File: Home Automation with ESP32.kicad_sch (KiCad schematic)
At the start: 0 parts

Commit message: Placed MCU (ESP32-WROOM-32) in Schematic
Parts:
- added U1: ESP32-WROOM-32, RF_Module:ESP32-WROOM-32, symbol RF_Module:ESP32-WROOM-32
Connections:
- new net: U1.1 (GND), U1.15 (GND), U1.38 (GND), U1.39 (GND)
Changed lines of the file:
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@@
 	(generator_version "9.0")
 	(paper "A4")
+	(symbol
+		(lib_id "RF_Module:ESP32-WROOM-32")
+		(at 246.38 68.58 0)
+		(unit 1)
+		(exclude_from_sim no)
+		(in_bom yes)
+		(on_board yes)
+		(dnp no)
+		(fields_autoplaced yes)
+		(property "Reference" "U1"
+			(at 248.5233 30.48 0)
+			(effects
+				(font
+					(size 1.27 1.27)
+				)
+				(justify left)
+			)
+		)
+		(property "Value" "ESP32-WROOM-32"
+			(at 248.5233 33.02 0)
+			(effects
+				(font
+					(size 1.27 1.27)
+				)
+				(justify left)
+			)
+		)
+		(property "Footprint" "RF_Module:ESP32-WROOM-32"
+			(at 246.38 106.68 0)
+			(effects
+				(font
+					(size 1.27 1.27)
+				)
+				(hide yes)
+			)
+		)
+		(property "Datasheet" "https://www.espressif.com/sites/default/files/documentation/esp32-wroom-32_datasheet_en.pdf"
+			(at 238.76 67.31 0)
+			(effects
+				(font
+					(size 1.27 1.27)
+				)
+				(hide yes)
+			)
+		)
+		(property "Description" "RF Module, ESP32-D0WDQ6 SoC, Wi-Fi 802.11b/g/n, Bluetooth, BLE, 32-bit, 2.7-3.6V, onboard antenna, SMD"
+			(at 246.38 68.58 0)
+			(effects
+				(font
+					(size 1.27 1.27)
+				)
+				(hide yes)
+			)
+		)
+		(pin "8"
+		)
+		(pin "23"
+		)
+		(pin "12"
+		)
+		(pin "27"
+		)
+		(pin "28"
+		)
+		(pin "33"
+		)
+		(pin "9"
+		)
+		(pin "7"
+		)
+		(pin "11"
+		)
+		(pin "36"
+		)
+		(pin "30"
+		)
+		(pin "10"
+		)
+		(pin "6"
+		)
+		(pin "31"
+		)
+		(pin "37"
+		)
+		(pin "5"
+		)
+		(pin "21"
+		)
+		(pin "22"
+		)
+		(pin "3"
+		)
+		(pin "4"
+		)
+		(pin "16"
+		)
+		(pin "13"
+		)
+		(pin "39"
+		)
+		(pin "32"
+		)
+		(pin "17"
+		)
+		(pin "20"
+		)
+		(pin "15"
+		)
+		(pin "24"
+		)
+		(pin "1"
+		)
+		(pin "34"
+		)
+		(pin "29"
+		)
+		(pin "14"
+		)
+		(pin "18"
+		)
+		(pin "25"
+		)
+		(pin "2"
+		)
+		(pin "38"
+		)
+		(pin "19"
+		)
+		(pin "35"
+		)
+		(pin "26"
+		)
+		(instances
+			(project ""
+				(path "/7438dd54-9f08-4599-aef6-4a86e3e5147b"
+					(reference "U1")
+					(unit 1)
+				)
+			)
+		)
+	)
 	(sheet_instances
 		(path "/"

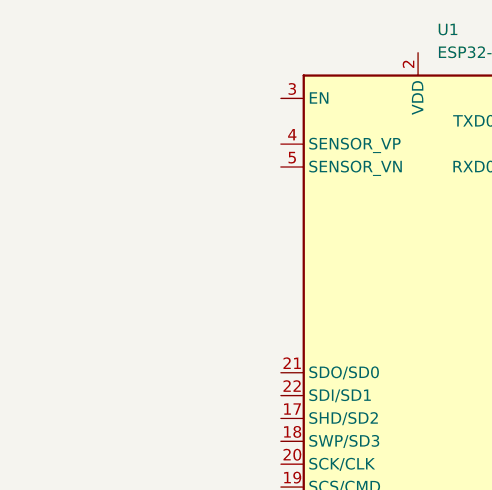
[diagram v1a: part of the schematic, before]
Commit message: Placed Isolator (PC817) in Schematic
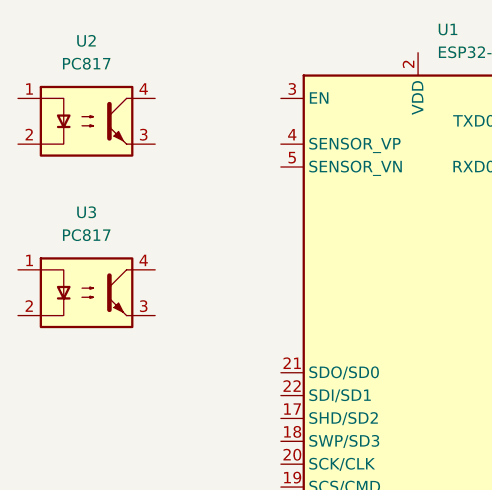
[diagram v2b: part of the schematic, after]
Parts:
- added U2, U3: PC817, Package_DIP:DIP-4_W7.62mm, symbol Isolator:PC817
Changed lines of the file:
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@@
 	(paper "A4")
+	(symbol
+		(lib_id "Isolator:PC817")
+		(at 209.55 40.64 0)
+		(unit 1)
+		(exclude_from_sim no)
+		(in_bom yes)
+		(on_board yes)
+		(dnp no)
+		(fields_autoplaced yes)
+		(property "Reference" "U2"
+			(at 209.55 31.75 0)
+			(effects
+				(font
+					(size 1.27 1.27)
+				)
+			)
+		)
+		(property "Value" "PC817"
+			(at 209.55 34.29 0)
+			(effects
+				(font
+					(size 1.27 1.27)
+				)
+			)
+		)
+		(property "Footprint" "Package_DIP:DIP-4_W7.62mm"
+			(at 204.47 45.72 0)
+			(effects
+				(font
+					(size 1.27 1.27)
+					(italic yes)
+				)
+				(justify left)
+				(hide yes)
+			)
+		)
+		(property "Datasheet" "http://www.soselectronic.cz/a_info/resource/d/pc817.pdf"
+			(at 209.55 40.64 0)
+			(effects
+				(font
+					(size 1.27 1.27)
+				)
+				(justify left)
+				(hide yes)
+			)
+		)
+		(property "Description" "DC Optocoupler, Vce 35V, CTR 50-300%, DIP-4"
+			(at 209.55 40.64 0)
+			(effects
+				(font
+					(size 1.27 1.27)
+				)
+				(hide yes)
+			)
+		)
+		(pin "3"
+		)
+		(pin "2"
+		)
+		(pin "1"
+		)
+		(pin "4"
+		)
+		(instances
+			(project ""
+				(path "/7438dd54-9f08-4599-aef6-4a86e3e5147b"
+					(reference "U2")
+					(unit 1)
+				)
+			)
+		)
+	)
+	(symbol
+		(lib_id "Isolator:PC817")
+		(at 209.55 59.69 0)
+		(unit 1)
+		(exclude_from_sim no)
+		(in_bom yes)
+		(on_board yes)
+		(dnp no)
+		(fields_autoplaced yes)
+		(property "Reference" "U3"
+			(at 209.55 50.8 0)
+			(effects
+				(font
+					(size 1.27 1.27)
+				)
+			)
+		)
+		(property "Value" "PC817"
+			(at 209.55 53.34 0)
+			(effects
+				(font
+					(size 1.27 1.27)
+				)
+			)
+		)
+		(property "Footprint" "Package_DIP:DIP-4_W7.62mm"
+			(at 204.47 64.77 0)
+			(effects
+				(font
+					(size 1.27 1.27)
+					(italic yes)
+				)
+				(justify left)
+				(hide yes)
+			)
+		)
+		(property "Datasheet" "http://www.soselectronic.cz/a_info/resource/d/pc817.pdf"
+			(at 209.55 59.69 0)
+			(effects
+				(font
+					(size 1.27 1.27)
+				)
+				(justify left)
+				(hide yes)
+			)
+		)
+		(property "Description" "DC Optocoupler, Vce 35V, CTR 50-300%, DIP-4"
+			(at 209.55 59.69 0)
+			(effects
+				(font
+					(size 1.27 1.27)
+				)
+				(hide yes)
+			)
+		)
+		(pin "3"
+		)
+		(pin "2"
+		)
+		(pin "1"
+		)
+		(pin "4"
+		)
+		(instances
+			(project "Home Automation with ESP32"
+				(path "/7438dd54-9f08-4599-aef6-4a86e3e5147b"
+					(reference "U3")
+					(unit 1)
+				)
+			)
+		)
+	)
 	(symbol
 		(lib_id "RF_Module:ESP32-WROOM-32")

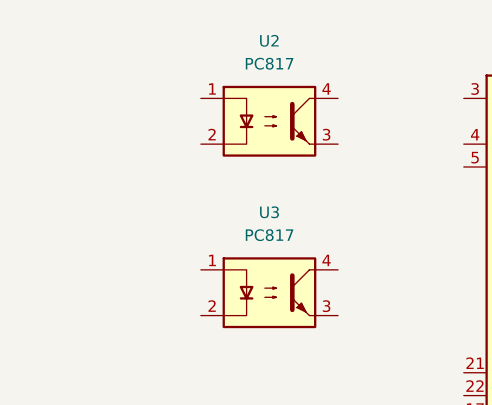
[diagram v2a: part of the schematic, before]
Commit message: Placed Linear Regulator (AMS1117-3.3) in Schematic
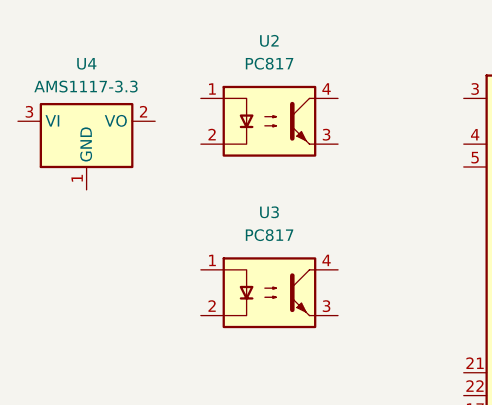
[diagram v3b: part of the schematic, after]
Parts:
- added U4: AMS1117-3.3, Package_TO_SOT_SMD:SOT-223-3_TabPin2, symbol Regulator_Linear:AMS1117-3.3
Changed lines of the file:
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@@
+	)
+	(symbol
+		(lib_id "Regulator_Linear:AMS1117-3.3")
+		(at 189.23 40.64 0)
+		(unit 1)
+		(exclude_from_sim no)
+		(in_bom yes)
+		(on_board yes)
+		(dnp no)
+		(fields_autoplaced yes)
+		(property "Reference" "U4"
+			(at 189.23 34.29 0)
+			(effects
+				(font
+					(size 1.27 1.27)
+				)
+			)
+		)
+		(property "Value" "AMS1117-3.3"
+			(at 189.23 36.83 0)
+			(effects
+				(font
+					(size 1.27 1.27)
+				)
+			)
+		)
+		(property "Footprint" "Package_TO_SOT_SMD:SOT-223-3_TabPin2"
+			(at 189.23 35.56 0)
+			(effects
+				(font
+					(size 1.27 1.27)
+				)
+				(hide yes)
+			)
+		)
+		(property "Datasheet" "http://www.advanced-monolithic.com/pdf/ds1117.pdf"
+			(at 191.77 46.99 0)
+			(effects
+				(font
+					(size 1.27 1.27)
+				)
+				(hide yes)
+			)
+		)
+		(property "Description" "1A Low Dropout regulator, positive, 3.3V fixed output, SOT-223"
+			(at 189.23 40.64 0)
+			(effects
+				(font
+					(size 1.27 1.27)
+				)
+				(hide yes)
+			)
+		)
+		(pin "2"
+		)
+		(pin "3"
+		)
+		(pin "1"
+		)
+		(instances
+			(project ""
+				(path "/7438dd54-9f08-4599-aef6-4a86e3e5147b"
+					(reference "U4")
+					(unit 1)
+				)
+			)
+		)
 	)
 	(symbol

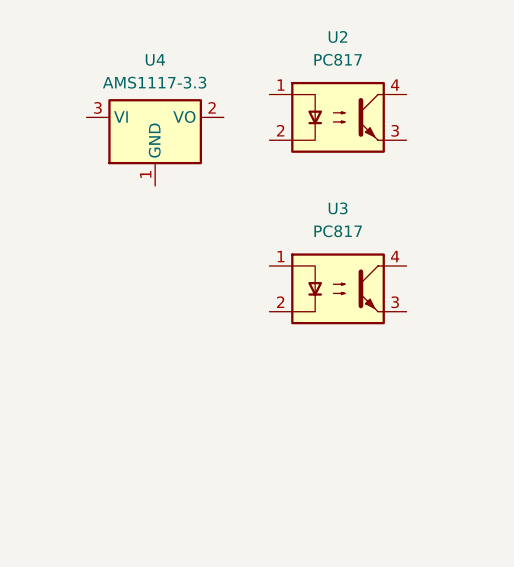
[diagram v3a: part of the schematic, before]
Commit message: Placed AC/DC Converter (HLK-PM01) in Schematic
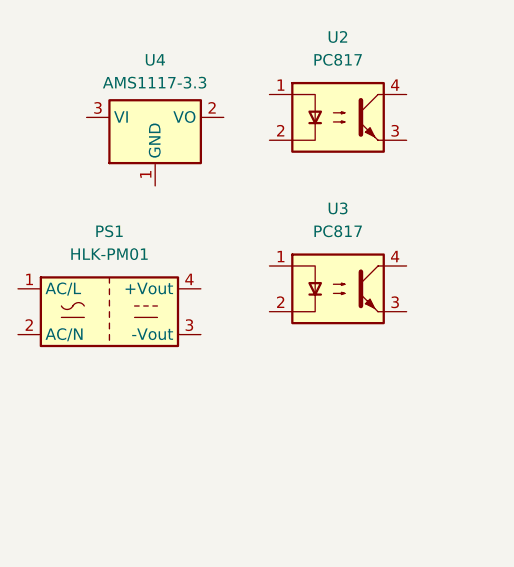
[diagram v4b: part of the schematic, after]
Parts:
- added PS1: HLK-PM01, Converter_ACDC:Converter_ACDC_Hi-Link_HLK-PMxx, symbol Converter_ACDC:HLK-PM01
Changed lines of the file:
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@@
+	)
+	(symbol
+		(lib_id "Converter_ACDC:HLK-PM01")
+		(at 184.15 62.23 0)
+		(unit 1)
+		(exclude_from_sim no)
+		(in_bom yes)
+		(on_board yes)
+		(dnp no)
+		(fields_autoplaced yes)
+		(property "Reference" "PS1"
+			(at 184.15 53.34 0)
+			(effects
+				(font
+					(size 1.27 1.27)
+				)
+			)
+		)
+		(property "Value" "HLK-PM01"
+			(at 184.15 55.88 0)
+			(effects
+				(font
+					(size 1.27 1.27)
+				)
+			)
+		)
+		(property "Footprint" "Converter_ACDC:Converter_ACDC_Hi-Link_HLK-PMxx"
+			(at 184.15 69.85 0)
+			(effects
+				(font
+					(size 1.27 1.27)
+				)
+				(hide yes)
+			)
+		)
+		(property "Datasheet" "https://h.hlktech.com/download/ACDC%E7%94%B5%E6%BA%90%E6%A8%A1%E5%9D%973W%E7%B3%BB%E5%88%97/1/%E6%B5%B7%E5%87%8C%E7%A7%913W%E7%B3%BB%E5%88%97%E7%94%B5%E6%BA%90%E6%A8%A1%E5%9D%97%E8%A7%84%E6%A0%BC%E4%B9%A6V2.8.pdf"
+			(at 194.31 71.12 0)
+			(effects
+				(font
+					(size 1.27 1.27)
+				)
+				(hide yes)
+			)
+		)
+		(property "Description" "Compact AC/DC board mount power module 3W 5V"
+			(at 184.15 62.23 0)
+			(effects
+				(font
+					(size 1.27 1.27)
+				)
+				(hide yes)
+			)
+		)
+		(pin "1"
+		)
+		(pin "4"
+		)
+		(pin "3"
+		)
+		(pin "2"
+		)
+		(instances
+			(project ""
+				(path "/7438dd54-9f08-4599-aef6-4a86e3e5147b"
+					(reference "PS1")
+					(unit 1)
+				)
+			)
+		)
 	)
 	(symbol

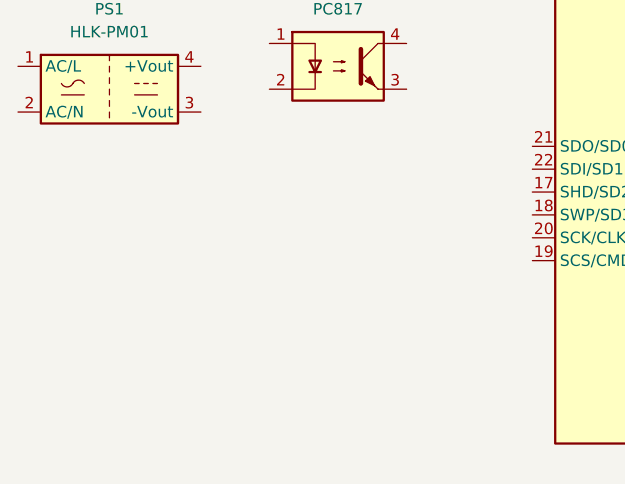
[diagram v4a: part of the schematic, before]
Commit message: Placed Power Relay (RAYEX-L90AS) in Schematic
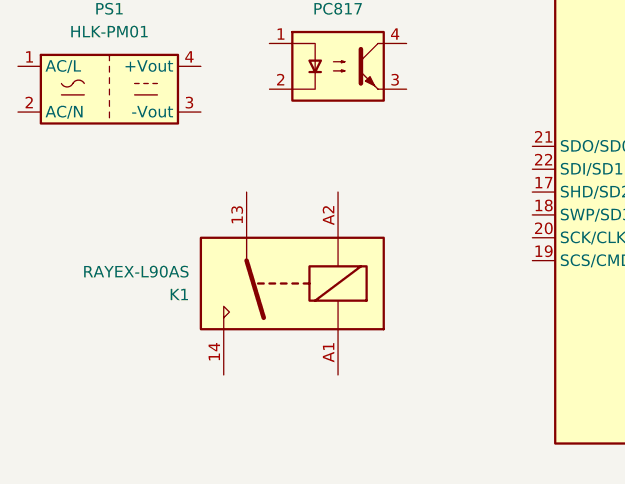
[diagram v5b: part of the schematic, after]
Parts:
- added K1: RAYEX-L90AS, Relay_THT:Relay_SPST_RAYEX-L90AS, symbol Relay:RAYEX-L90AS
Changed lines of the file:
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@@
 	(paper "A4")
+	(symbol
+		(lib_id "Relay:RAYEX-L90AS")
+		(at 204.47 83.82 180)
+		(unit 1)
+		(exclude_from_sim no)
+		(in_bom yes)
+		(on_board yes)
+		(dnp no)
+		(property "Reference" "K1"
+			(at 193.04 85.0901 0)
+			(effects
+				(font
+					(size 1.27 1.27)
+				)
+				(justify left)
+			)
+		)
+		(property "Value" "RAYEX-L90AS"
+			(at 193.04 82.5501 0)
+			(effects
+				(font
+					(size 1.27 1.27)
+				)
+				(justify left)
+			)
+		)
+		(property "Footprint" "Relay_THT:Relay_SPST_RAYEX-L90AS"
+			(at 193.04 82.55 0)
+			(effects
+				(font
+					(size 1.27 1.27)
+				)
+				(justify left)
+				(hide yes)
+			)
+		)
+		(property "Datasheet" "https://a3.sofastcdn.com/attachment/7jioKBjnRiiSrjrjknRiwS77gwbf3zmp/L90-SERIES.pdf"
+			(at 186.69 80.01 0)
+			(effects
+				(font
+					(size 1.27 1.27)
+				)
+				(justify left)
+				(hide yes)
+			)
+		)
+		(property "Description" "Power relay, Without Common Terminal between coil terminals, NO, SPST, 30A"
+			(at 204.47 83.82 0)
+			(effects
+				(font
+					(size 1.27 1.27)
+				)
+				(hide yes)
+			)
+		)
+		(pin "14"
+		)
+		(pin "A1"
+		)
+		(pin "13"
+		)
+		(pin "A2"
+		)
+		(instances
+			(project ""
+				(path "/7438dd54-9f08-4599-aef6-4a86e3e5147b"
+					(reference "K1")
+					(unit 1)
+				)
+			)
+		)
+	)
 	(symbol
 		(lib_id "Isolator:PC817")

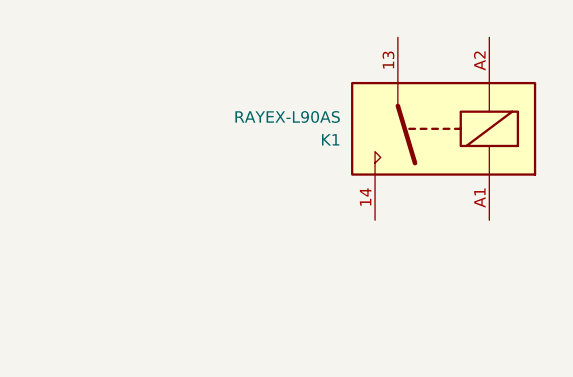
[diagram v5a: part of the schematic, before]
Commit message: Placed SPDT Power Relay (pr13-5v-450-1c) in Schematic
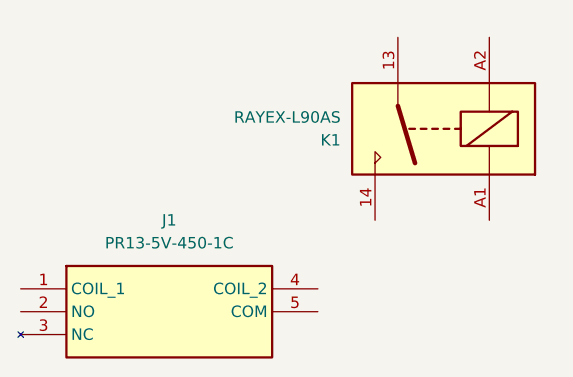
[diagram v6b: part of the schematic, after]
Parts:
- added J1: PR13-5V-450-1C, PR135V4501C, symbol PR13-5V-450-1C:PR13-5V-450-1C
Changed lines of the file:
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@@
+	)
+	(symbol
+		(lib_id "PR13-5V-450-1C:PR13-5V-450-1C")
+		(at 157.48 101.6 0)
+		(unit 1)
+		(exclude_from_sim no)
+		(in_bom yes)
+		(on_board yes)
+		(dnp no)
+		(fields_autoplaced yes)
+		(property "Reference" "J1"
+			(at 173.99 93.98 0)
+			(effects
+				(font
+					(size 1.27 1.27)
+				)
+			)
+		)
+		(property "Value" "PR13-5V-450-1C"
+			(at 173.99 96.52 0)
+			(effects
+				(font
+					(size 1.27 1.27)
+				)
+			)
+		)
+		(property "Footprint" "PR135V4501C"
+			(at 186.69 196.52 0)
+			(effects
+				(font
+					(size 1.27 1.27)
+				)
+				(justify left top)
+				(hide yes)
+			)
+		)
+		(property "Datasheet" "https://www.sameskydevices.com/product/resource/pr13.pdf"
+			(at 186.69 296.52 0)
+			(effects
+				(font
+					(size 1.27 1.27)
+				)
+				(justify left top)
+				(hide yes)
+			)
+		)
+		(property "Description" "19 x 15.5 x 15.8 mm, 5 V, 10 A, SPDT (1 Form C), Power Relay"
+			(at 157.48 101.6 0)
+			(effects
+				(font
+					(size 1.27 1.27)
+				)
+				(hide yes)
+			)
+		)
+		(property "Height" "16.1"
+			(at 186.69 496.52 0)
+			(effects
+				(font
+					(size 1.27 1.27)
+				)
+				(justify left top)
+				(hide yes)
+			)
+		)
+		(property "Manufacturer_Name" "Same Sky"
+			(at 186.69 596.52 0)
+			(effects
+				(font
+					(size 1.27 1.27)
+				)
+				(justify left top)
+				(hide yes)
+			)
+		)
+		(property "Manufacturer_Part_Number" "PR13-5V-450-1C"
+			(at 186.69 696.52 0)
+			(effects
+				(font
+					(size 1.27 1.27)
+				)
+				(justify left top)
+				(hide yes)
+			)
+		)
+		(property "Mouser Part Number" "179-PR13-5V-450-1C"
+			(at 186.69 796.52 0)
+			(effects
+				(font
+					(size 1.27 1.27)
+				)
+				(justify left top)
+				(hide yes)
+			)
+		)
+		(property "Mouser Price/Stock" "https://www.mouser.co.uk/ProductDetail/CUI-Devices/PR13-5V-450-1C?qs=T%252BzbugeAwjjEdhOl%2F9q49A%3D%3D"
+			(at 186.69 896.52 0)
+			(effects
+				(font
+					(size 1.27 1.27)
+				)
+				(justify left top)
+				(hide yes)
+			)
+		)
+		(property "Arrow Part Number" "PR13-5V-450-1C"
+			(at 186.69 996.52 0)
+			(effects
+				(font
+					(size 1.27 1.27)
+				)
+				(justify left top)
+				(hide yes)
+			)
+		)
+		(property "Arrow Price/Stock" "https://www.arrow.com/en/products/pr13-5v-450-1c/cui-devices?region=nac"
+			(at 186.69 1096.52 0)
+			(effects
+				(font
+					(size 1.27 1.27)
+				)
+				(justify left top)
+				(hide yes)
+			)
+		)
+		(pin "1"
+		)
+		(pin "3"
+		)
+		(pin "5"
+		)
+		(pin "2"
+		)
+		(pin "4"
+		)
+		(instances
+			(project ""
+				(path "/7438dd54-9f08-4599-aef6-4a86e3e5147b"
+					(reference "J1")
+					(unit 1)
+				)
+			)
+		)
 	)
 	(symbol

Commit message: Placed Transistor (S8050) in Schematic
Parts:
- added Q1, Q2: S8050, Package_TO_SOT_THT:TO-92_Inline, symbol Transistor_BJT:S8050
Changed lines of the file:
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@@
 	(paper "A4")
+	(symbol
+		(lib_id "Transistor_BJT:S8050")
+		(at 210.82 106.68 0)
+		(unit 1)
+		(exclude_from_sim no)
+		(in_bom yes)
+		(on_board yes)
+		(dnp no)
+		(fields_autoplaced yes)
+		(property "Reference" "Q1"
+			(at 215.9 105.4099 0)
+			(effects
+				(font
+					(size 1.27 1.27)
+				)
+				(justify left)
+			)
+		)
+		(property "Value" "S8050"
+			(at 215.9 107.9499 0)
+			(effects
+				(font
+					(size 1.27 1.27)
+				)
+				(justify left)
+			)
+		)
+		(property "Footprint" "Package_TO_SOT_THT:TO-92_Inline"
+			(at 215.9 108.585 0)
+			(effects
+				(font
+					(size 1.27 1.27)
+					(italic yes)
+				)
+				(justify left)
+				(hide yes)
+			)
+		)
+		(property "Datasheet" "http://www.unisonic.com.tw/datasheet/S8050.pdf"
+			(at 210.82 106.68 0)
+			(effects
+				(font
+					(size 1.27 1.27)
+				)
+				(justify left)
+				(hide yes)
+			)
+		)
+		(property "Description" "0.7A Ic, 20V Vce, Low Voltage High Current NPN Transistor, TO-92"
+			(at 210.82 106.68 0)
+			(effects
+				(font
+					(size 1.27 1.27)
+				)
+				(hide yes)
+			)
+		)
+		(pin "3"
+		)
+		(pin "2"
+		)
+		(pin "1"
+		)
+		(instances
+			(project ""
+				(path "/7438dd54-9f08-4599-aef6-4a86e3e5147b"
+					(reference "Q1")
+					(unit 1)
+				)
+			)
+		)
+	)
 	(symbol
 		(lib_id "Relay:RAYEX-L90AS")
@@
 					(unit 1)
 				)
+			)
+		)
+	)
+	(symbol
+		(lib_id "Transistor_BJT:S8050")
+		(at 210.82 121.92 0)
+		(unit 1)
+		(exclude_from_sim no)
+		(in_bom yes)
+		(on_board yes)
+		(dnp no)
+		(fields_autoplaced yes)
+		(property "Reference" "Q2"
+			(at 215.9 120.6499 0)
+			(effects
+				(font
+					(size 1.27 1.27)
+				)
+				(justify left)
+			)
+		)
+		(property "Value" "S8050"
+			(at 215.9 123.1899 0)
+			(effects
+				(font
+					(size 1.27 1.27)
+				)
+				(justify left)
+			)
+		)
+		(property "Footprint" "Package_TO_SOT_THT:TO-92_Inline"
+			(at 215.9 123.825 0)
+			(effects
+				(font
+					(size 1.27 1.27)
+					(italic yes)
+				)
+				(justify left)
+				(hide yes)
+			)
+		)
+		(property "Datasheet" "http://www.unisonic.com.tw/datasheet/S8050.pdf"
+			(at 210.82 121.92 0)
+			(effects
+				(font
+					(size 1.27 1.27)
+				)
+				(justify left)
+				(hide yes)
+			)
+		)
+		(property "Description" "0.7A Ic, 20V Vce, Low Voltage High Current NPN Transistor, TO-92"
+			(at 210.82 121.92 0)
+			(effects
+				(font
+					(size 1.27 1.27)
+				)
+				(hide yes)
+			)
+		)
+		(pin "3"
+		)
+		(pin "2"
+		)
+		(pin "1"
+		)
+		(instances
+			(project "Home Automation with ESP32"
+				(path "/7438dd54-9f08-4599-aef6-4a86e3e5147b"
+					(reference "Q2")
+					(unit 1)
+				)

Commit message: Placed SW_PUSH in Schematic
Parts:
- added SW1, SW2: SW_Push, symbol Switch:SW_Push
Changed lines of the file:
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@@
+	)
+	(symbol
+		(lib_id "Switch:SW_Push")
+		(at 181.61 124.46 0)
+		(unit 1)
+		(exclude_from_sim no)
+		(in_bom yes)
+		(on_board yes)
+		(dnp no)
+		(fields_autoplaced yes)
+		(property "Reference" "SW1"
+			(at 181.61 116.84 0)
+			(effects
+				(font
+					(size 1.27 1.27)
+				)
+			)
+		)
+		(property "Value" "SW_Push"
+			(at 181.61 119.38 0)
+			(effects
+				(font
+					(size 1.27 1.27)
+				)
+			)
+		)
+		(property "Footprint" ""
+			(at 181.61 119.38 0)
+			(effects
+				(font
+					(size 1.27 1.27)
+				)
+				(hide yes)
+			)
+		)
+		(property "Datasheet" "~"
+			(at 181.61 119.38 0)
+			(effects
+				(font
+					(size 1.27 1.27)
+				)
+				(hide yes)
+			)
+		)
+		(property "Description" "Push button switch, generic, two pins"
+			(at 181.61 124.46 0)
+			(effects
+				(font
+					(size 1.27 1.27)
+				)
+				(hide yes)
+			)
+		)
+		(pin "2"
+		)
+		(pin "1"
+		)
+		(instances
+			(project ""
+				(path "/7438dd54-9f08-4599-aef6-4a86e3e5147b"
+					(reference "SW1")
+					(unit 1)
+				)
+			)
+		)
 	)
 	(symbol
@@
 					(unit 1)
 				)
+			)
+		)
+	)
+	(symbol
+		(lib_id "Switch:SW_Push")
+		(at 194.31 124.46 0)
+		(unit 1)
+		(exclude_from_sim no)
+		(in_bom yes)
+		(on_board yes)
+		(dnp no)
+		(fields_autoplaced yes)
+		(property "Reference" "SW2"
+			(at 194.31 116.84 0)
+			(effects
+				(font
+					(size 1.27 1.27)
+				)
+			)
+		)
+		(property "Value" "SW_Push"
+			(at 194.31 119.38 0)
+			(effects
+				(font
+					(size 1.27 1.27)
+				)
+			)
+		)
+		(property "Footprint" ""
+			(at 194.31 119.38 0)
+			(effects
+				(font
+					(size 1.27 1.27)
+				)
+				(hide yes)
+			)
+		)
+		(property "Datasheet" "~"
+			(at 194.31 119.38 0)
+			(effects
+				(font
+					(size 1.27 1.27)
+				)
+				(hide yes)
+			)
+		)
+		(property "Description" "Push button switch, generic, two pins"
+			(at 194.31 124.46 0)
+			(effects
+				(font
+					(size 1.27 1.27)
+				)
+				(hide yes)
+			)
+		)
+		(pin "2"
+		)
+		(pin "1"
+		)
+		(instances
+			(project "Home Automation with ESP32"
+				(path "/7438dd54-9f08-4599-aef6-4a86e3e5147b"
+					(reference "SW2")
+					(unit 1)
+				)
